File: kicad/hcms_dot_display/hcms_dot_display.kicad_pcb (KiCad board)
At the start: 2 copper layers, 35.5 x 19.8 mm, 35 parts, among them J1 Conn_01x13, J2 USB_C_Receptacle_USB2.0, J3 Conn_01x13, Q1 Q_PMOS_DSG, Q2 Q_PMOS_DSG, Q3 Q_PMOS_DSG, Q4 Q_PMOS_DSG, Q5 Q_PMOS_DSG, U1 ATtiny824-SSF, U2 FT231XS

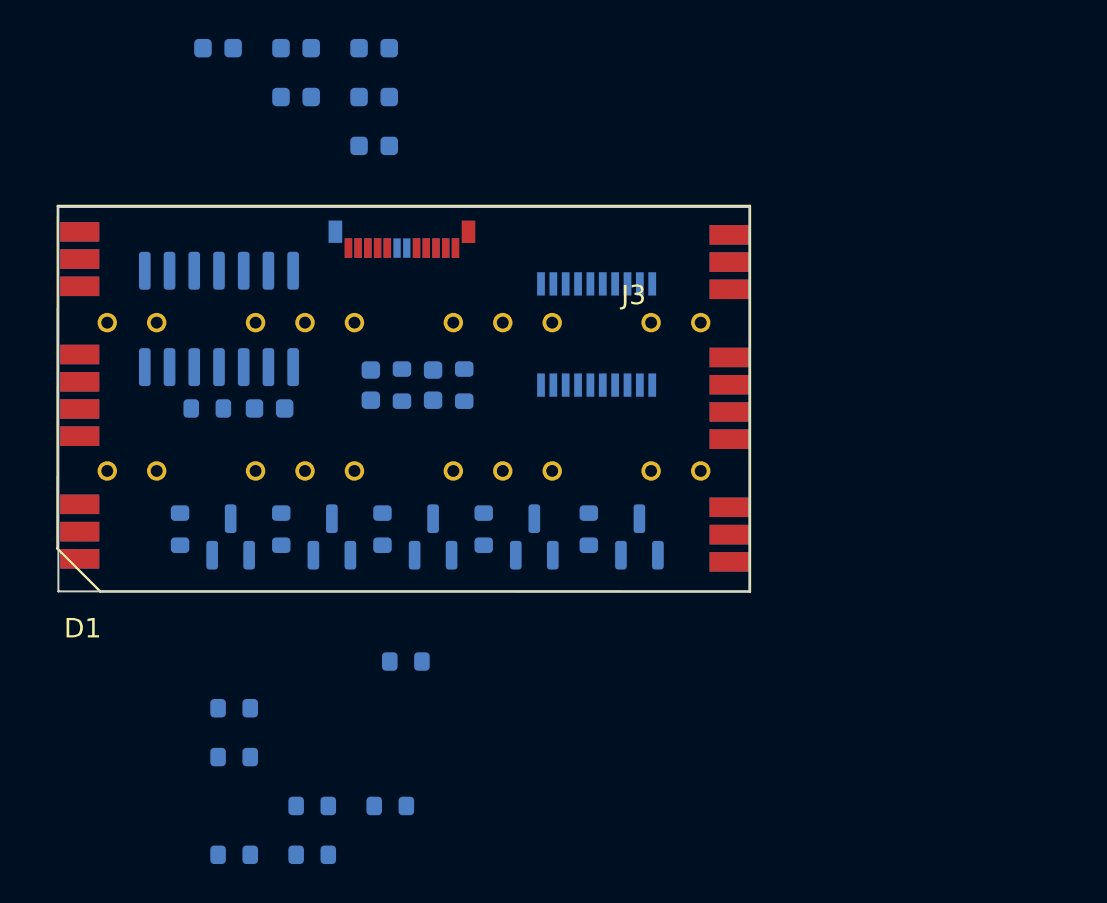
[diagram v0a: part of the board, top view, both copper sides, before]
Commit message: Added PNs for push button and pot with basic footprints, updated some resistor values
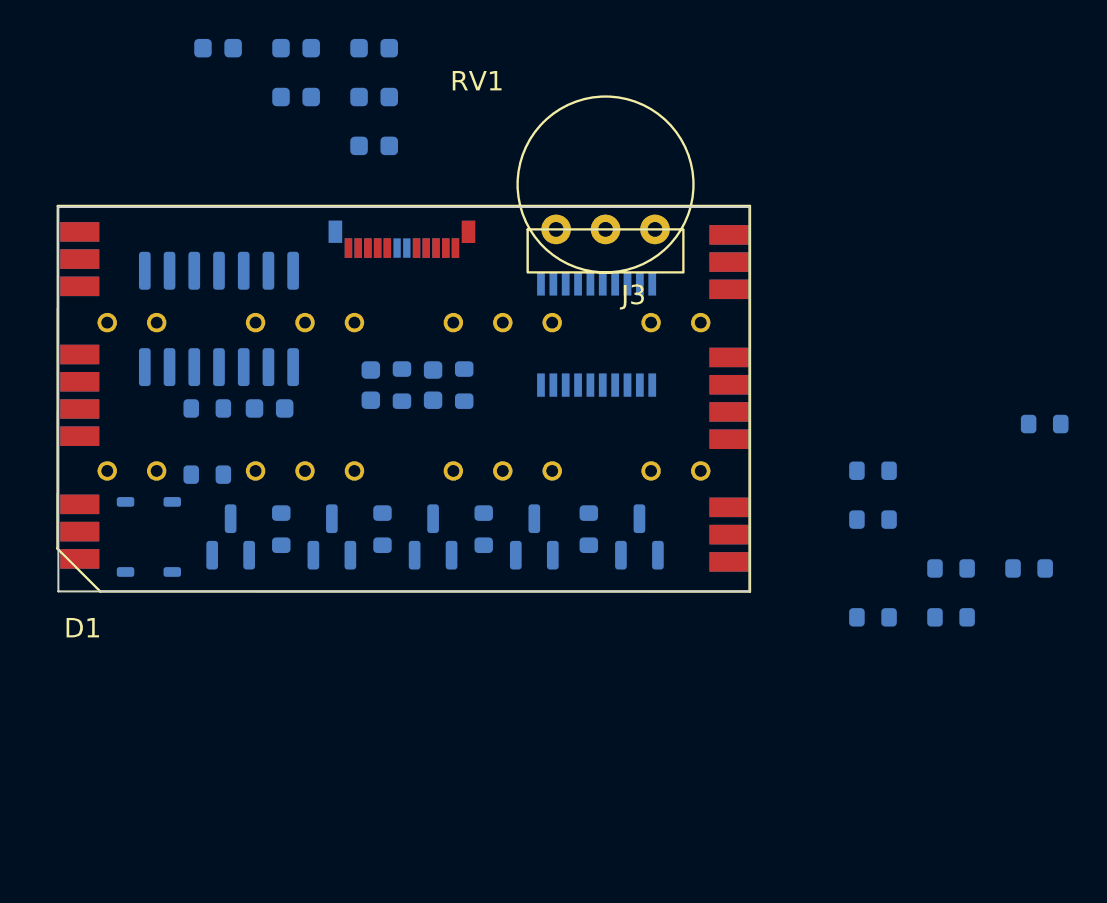
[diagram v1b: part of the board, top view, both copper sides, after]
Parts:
- added RV1: R_Potentiometer, hcms:3352T-1-503LF, F.Cu at (162.9, 97.4)
- added SW1: SW_Push, hcms:R-667845, B.Cu at (139.4, 113.2)
- R10, R11, R12, R13, R14: value R -> 200
- R3: value R -> 330
- moved R2 35.0 mm to (180.6, 114.8)
- moved R4 35.0 mm to (180.6, 117.3)
- moved R1 35.0 mm to (185.4, 107.4)
- moved R3 35.0 mm to (176.6, 112.3)
- moved R5 35.0 mm to (184.6, 114.8)
- moved R6 35.0 mm to (176.6, 117.3)
- moved R7 35.0 mm to (176.6, 109.8)
- moved R12 3.13 mm to (142.4, 110.0), turned to 180 degrees
- turned R13 to -90 degrees
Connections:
- J2 pad A4: +5V -> Net-(J2-PadA4)
- J2 pad A9: +5V -> Net-(J2-PadA4)
- J2 pad B4: +5V -> Net-(J2-PadA4)
- J2 pad B9: +5V -> Net-(J2-PadA4)
- R1 pad 1: Net-(D1-Pad26)_1 -> Net-(D1-Pad26)
- R2 pad 1: Net-(D1-Pad26)_1 -> Net-(D1-Pad26)
- R6 pad 1: Net-(D1-Pad26) -> Net-(D1-Pad26)_1
- R7 pad 1: Net-(D1-Pad26) -> Net-(D1-Pad26)_1

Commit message: layout
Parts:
- moved R5 46.7 mm to (142.8, 94.0)
- moved R1 46.4 mm to (139.0, 106.8)
- moved R3 42.4 mm to (138.4, 93.8)
- moved R2 42.1 mm to (139.0, 108.4)
- moved R4 41.6 mm to (146.2, 94.0)
- moved C7 25.0 mm to (157.8, 108.2)
- moved C9 20.4 mm to (154.6, 108.2)
- moved R7 15.7 mm to (161.0, 108.2)
- moved R6 15.4 mm to (164.2, 108.2)
- moved C6 13.3 mm to (158.6, 94.6)
- moved C8 11.9 mm to (162.6, 93.2)
- moved C1 9.73 mm to (140.0, 97.4)
- moved C2 9.05 mm to (143.0, 97.4)
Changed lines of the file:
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@@
   )
   (footprint "Capacitor_SMD:C_0603_1608Metric" (layer "B.Cu")
-    (at 142.951904 88.09 180)
+    (at 157.8 108.2 180)
     (descr "Capacitor SMD 0603 (1608 Metric), square (rectangular) end terminal, IPC_7351 nominal, (Body size source: IPC-SM-782 page 76, https://www.pcb-3d.com/wordpress/wp-content/uploads/ipc-sm-782a_amendment_1_and_2.pdf), generated with kicad-footprint-generator")
     (tags "capacitor")
@@
   )
   (footprint "Capacitor_SMD:C_0603_1608Metric" (layer "B.Cu")
-    (at 150.971904 88.09 180)
+    (at 154.6 108.2 180)
     (descr "Capacitor SMD 0603 (1608 Metric), square (rectangular) end terminal, IPC_7351 nominal, (Body size source: IPC-SM-782 page 76, https://www.pcb-3d.com/wordpress/wp-content/uploads/ipc-sm-782a_amendment_1_and_2.pdf), generated with kicad-footprint-generator")
     (tags "capacitor")
@@
   )
   (footprint "Resistor_SMD:R_0603_1608Metric" (layer "B.Cu")
-    (at 176.6 117.33 180)
+    (at 164.225 108.2 180)
     (descr "Resistor SMD 0603 (1608 Metric), square (rectangular) end terminal, IPC_7351 nominal, (Body size source: IPC-SM-782 page 72, https://www.pcb-3d.com/wordpress/wp-content/uploads/ipc-sm-782a_amendment_1_and_2.pdf), generated with kicad-footprint-generator")
     (tags "resistor")
@@
   )
   (footprint "Resistor_SMD:R_0603_1608Metric" (layer "B.Cu")
-    (at 176.6 112.31 180)
+    (at 138.4 93.8 180)
     (descr "Resistor SMD 0603 (1608 Metric), square (rectangular) end terminal, IPC_7351 nominal, (Body size source: IPC-SM-782 page 72, https://www.pcb-3d.com/wordpress/wp-content/uploads/ipc-sm-782a_amendment_1_and_2.pdf), generated with kicad-footprint-generator")
     (tags "resistor")
@@
   )
   (footprint "Capacitor_SMD:C_0603_1608Metric" (layer "B.Cu")
-    (at 146.961904 88.09 180)
+    (at 158.6 94.6 180)
     (descr "Capacitor SMD 0603 (1608 Metric), square (rectangular) end terminal, IPC_7351 nominal, (Body size source: IPC-SM-782 page 76, https://www.pcb-3d.com/wordpress/wp-content/uploads/ipc-sm-782a_amendment_1_and_2.pdf), generated with kicad-footprint-generator")
     (tags "capacitor")
@@
   )
   (footprint "Resistor_SMD:R_0603_1608Metric" (layer "B.Cu")
-    (at 180.61 117.33 180)
+    (at 146.2 94 180)
     (descr "Resistor SMD 0603 (1608 Metric), square (rectangular) end terminal, IPC_7351 nominal, (Body size source: IPC-SM-782 page 72, https://www.pcb-3d.com/wordpress/wp-content/uploads/ipc-sm-782a_amendment_1_and_2.pdf), generated with kicad-footprint-generator")
     (tags "resistor")
@@
   )
   (footprint "Capacitor_SMD:C_0603_1608Metric" (layer "B.Cu")
-    (at 150.971904 90.6 180)
+    (at 162.6 93.2 180)
     (descr "Capacitor SMD 0603 (1608 Metric), square (rectangular) end terminal, IPC_7351 nominal, (Body size source: IPC-SM-782 page 76, https://www.pcb-3d.com/wordpress/wp-content/uploads/ipc-sm-782a_amendment_1_and_2.pdf), generated with kicad-footprint-generator")
     (tags "capacitor")
@@
   )
   (footprint "Capacitor_SMD:C_0603_1608Metric" (layer "B.Cu")
-    (at 146.961904 90.6 180)
+    (at 140 97.4 180)
     (descr "Capacitor SMD 0603 (1608 Metric), square (rectangular) end terminal, IPC_7351 nominal, (Body size source: IPC-SM-782 page 76, https://www.pcb-3d.com/wordpress/wp-content/uploads/ipc-sm-782a_amendment_1_and_2.pdf), generated with kicad-footprint-generator")
     (tags "capacitor")
@@
   )
   (footprint "Resistor_SMD:R_0603_1608Metric" (layer "B.Cu")
-    (at 176.6 109.8 180)
+    (at 161 108.2 180)
     (descr "Resistor SMD 0603 (1608 Metric), square (rectangular) end terminal, IPC_7351 nominal, (Body size source: IPC-SM-782 page 72, https://www.pcb-3d.com/wordpress/wp-content/uploads/ipc-sm-782a_amendment_1_and_2.pdf), generated with kicad-footprint-generator")
     (tags "resistor")
@@
   )
   (footprint "Resistor_SMD:R_0603_1608Metric" (layer "B.Cu")
-    (at 180.61 114.82 180)
+    (at 139 108.4 180)
     (descr "Resistor SMD 0603 (1608 Metric), square (rectangular) end terminal, IPC_7351 nominal, (Body size source: IPC-SM-782 page 72, https://www.pcb-3d.com/wordpress/wp-content/uploads/ipc-sm-782a_amendment_1_and_2.pdf), generated with kicad-footprint-generator")
     (tags "resistor")
@@
   )
   (footprint "Capacitor_SMD:C_0603_1608Metric" (layer "B.Cu")
-    (at 150.971904 93.11 180)
+    (at 143 97.4 180)
     (descr "Capacitor SMD 0603 (1608 Metric), square (rectangular) end terminal, IPC_7351 nominal, (Body size source: IPC-SM-782 page 76, https://www.pcb-3d.com/wordpress/wp-content/uploads/ipc-sm-782a_amendment_1_and_2.pdf), generated with kicad-footprint-generator")
     (tags "capacitor")
@@
   )
   (footprint "Resistor_SMD:R_0603_1608Metric" (layer "B.Cu")
-    (at 184.62 114.82 180)
+    (at 142.8 94 180)
     (descr "Resistor SMD 0603 (1608 Metric), square (rectangular) end terminal, IPC_7351 nominal, (Body size source: IPC-SM-782 page 72, https://www.pcb-3d.com/wordpress/wp-content/uploads/ipc-sm-782a_amendment_1_and_2.pdf), generated with kicad-footprint-generator")
     (tags "resistor")
@@
   )
   (footprint "Resistor_SMD:R_0603_1608Metric" (layer "B.Cu")
-    (at 185.42 107.4 180)
-    (descr "Resistor SMD 0603 (1608 Metric), square (rectangular) end terminal, IPC_7351 nominal, (Body size source: IPC-SM-782 page 72, https://www.pcb-3d.com/wordpress/wp-content/uploads/ipc-sm-782a_amendment_1_and_2.pdf), generated with kicad-footprint-generator")
-    (tags "resistor")
+    (at 139 106.8 180)
+    (descr "Resistor SMD 0603 (1608 Metric), square (rectangular) end terminal, IPC_7351 nominal, (Body size source: IPC-SM-782 page 72, https://www.pcb-3d.com/wordpress/wp-content/uploads/ipc-sm-782a_amendment_1_and_2.pdf), generated with kicad-footprint-generator")
+    (tags "resistor")

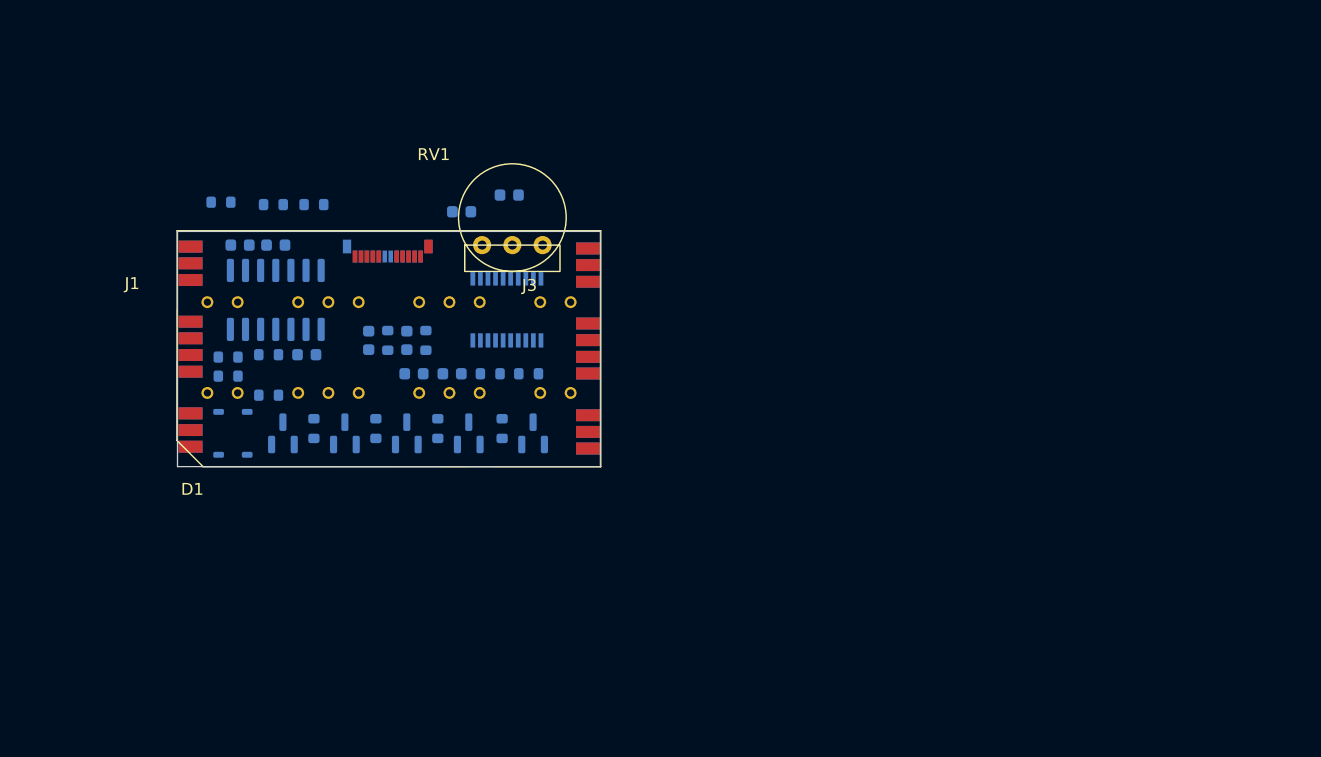
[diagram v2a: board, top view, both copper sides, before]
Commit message: Updated dot matrix footprint, experimented with stacked control board design
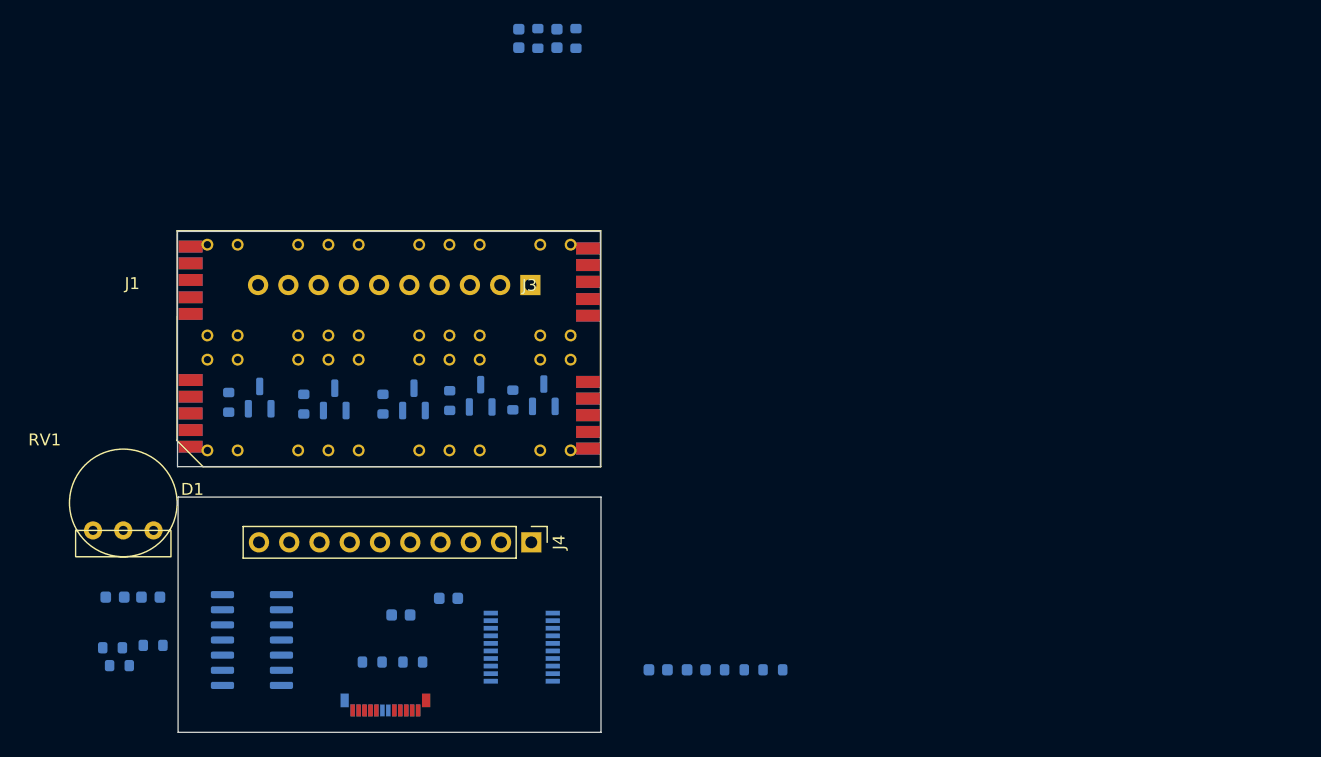
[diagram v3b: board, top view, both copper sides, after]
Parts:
- removed C3: 100nF, Capacitor_SMD:C_0603_1608Metric
- removed R3: 330, Resistor_SMD:R_0603_1608Metric
- removed SW1: SW_Push, hcms:R-667845
- added J4: Conn_01x13, Connector_PinHeader_2.54mm:PinHeader_1x10_P2.54mm_Vertical, F.Cu at (164.4, 122.3)
- added J5: Conn_01x13, Connector_PinHeader_2.54mm:PinHeader_1x10_P2.54mm_Vertical, B.Cu at (164.4, 100.8)
- R1, R6: value R -> 0
- R15: value R -> 1k
- R2, R7: value R -> DNP
- moved RV1 40.5 mm to (130.2, 121.3)
- moved R4 39.3 mm to (154.5, 132.4)
- moved R5 39.3 mm to (151.1, 132.4)
- moved J2 38.1 mm to (152.2, 136.5)
- moved C6 34.2 mm to (153.5, 128.4)
- moved C8 34.2 mm to (157.5, 127.0)
- moved C7 32.2 mm to (178.3, 133.1)
- moved C9 32.2 mm to (175.1, 133.1)
- moved R6 32.2 mm to (184.7, 133.1)
- moved R7 32.2 mm to (181.5, 133.1)
- moved C1 31.4 mm to (129.5, 127.0)
- moved C2 31.4 mm to (132.5, 127.0)
- moved U1 28.6 mm to (141.0, 130.6), turned to 0 degrees
- moved U2 28.4 mm to (163.7, 131.2), turned to 180 degrees
- moved C4 28.3 mm to (166.6, 80.0)
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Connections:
- R1 pad 1: Net-(D1-Pad26) -> Net-(D1-Pad26A)
- R2 pad 1: Net-(D1-Pad26) -> Net-(D1-Pad26A)
- R6 pad 1: Net-(D1-Pad26)_1 -> Net-(R6-Pad1)
- R7 pad 1: Net-(D1-Pad26)_1 -> Net-(R6-Pad1)
- U1 pad 10: /UPDI -> /MCU_COL_3
- U1 pad 11: /MCU_COL_1 -> /MCU_COL_2
- U1 pad 12: /MCU_COL_2 -> /MCU_COL_1
- U1 pad 13: /MCU_COL_3 -> /UPDI
- U1 pad 2: /MCU_COL_4 -> /MCU_DATA
- U1 pad 3: /MCU_COL_5 -> unconnected-(U1-Pad3)
- U1 pad 4: /POT -> /nBLNK
- U1 pad 5: /CLK -> unconnected-(U1-Pad5)
- U1 pad 6: /nBLNK -> /POT
- U1 pad 7: unconnected-(U1-Pad7) -> /CLK
- U1 pad 8: unconnected-(U1-Pad8) -> /MCU_COL_5
- U1 pad 9: /MCU_DATA -> /MCU_COL_4
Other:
- board size 35.5 x 19.8 mm -> 35.6 x 42.1 mm

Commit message: Cleaned up layout strat
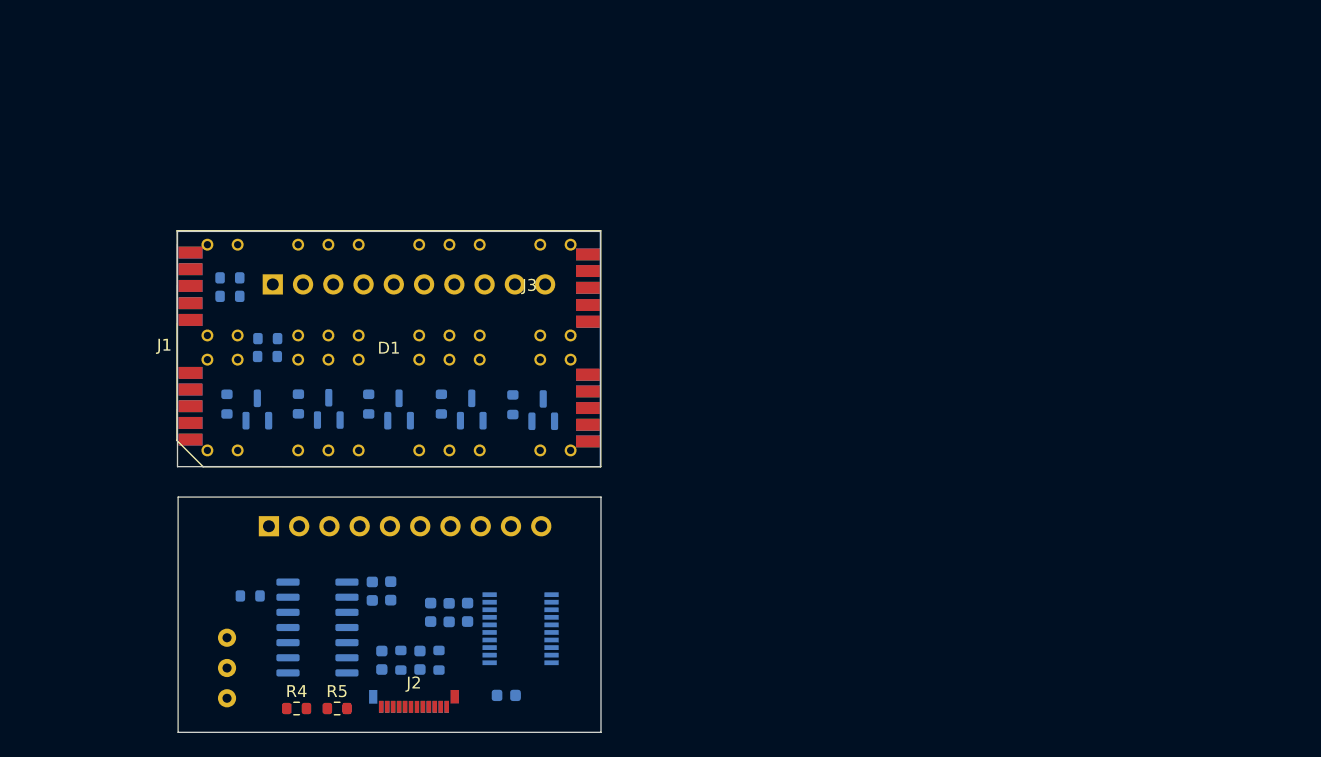
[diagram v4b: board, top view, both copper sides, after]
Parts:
- J2, R4, R5: moved to F.Cu
- J4: value Conn_01x13 -> Conn_01x10_Female; moved to B.Cu
- J5: value Conn_01x13 -> Conn_01x10_Male
- RV1: moved to B.Cu
- moved R6 55.3 mm to (139.2, 101.7)
- moved R7 53.6 mm to (139.2, 100.2)
- moved C4 53.5 mm to (155.1, 132.2)
- moved C5 53.5 mm to (151.9, 132.2)
- moved R8 53.5 mm to (156.7, 132.2)
- moved R9 53.5 mm to (153.5, 132.2)
- moved J4 30.7 mm to (142.8, 100.7)
- moved J5 29.9 mm to (142.4, 121.0), turned to -90 degrees
- moved R1 29.0 mm to (142.3, 105.2)
- moved R2 28.8 mm to (142.3, 106.8)
- moved C1 21.6 mm to (151.1, 126.5), turned to -90 degrees
- moved C7 21.3 mm to (157.6, 128.2), turned to 90 degrees
- moved C2 20.2 mm to (152.7, 126.4), turned to -90 degrees
- moved C9 16.7 mm to (159.1, 128.2), turned to 90 degrees
- moved RV1 14.5 mm to (138.9, 132.9), turned to -90 degrees
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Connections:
- J4 pad 1: unconnected-(J4-Pad1) -> /nBLNK
- J4 pad 10: unconnected-(J4-Pad10) -> GND
- J4 pad 2: unconnected-(J4-Pad2) -> /MCU_DATA
- J4 pad 3: unconnected-(J4-Pad3) -> /CLK
- J4 pad 4: unconnected-(J4-Pad4) -> /MCU_COL_5
- J4 pad 5: unconnected-(J4-Pad5) -> /MCU_COL_4
- J4 pad 6: unconnected-(J4-Pad6) -> /MCU_COL_3
- J4 pad 7: unconnected-(J4-Pad7) -> /MCU_COL_2
- J4 pad 8: unconnected-(J4-Pad8) -> /MCU_COL_1
- J4 pad 9: unconnected-(J4-Pad9) -> +5V
- J5 pad 1: unconnected-(J5-Pad1) -> /nBLNK
- J5 pad 10: unconnected-(J5-Pad10) -> GND
- J5 pad 2: unconnected-(J5-Pad2) -> /MCU_DATA
- J5 pad 3: unconnected-(J5-Pad3) -> /CLK
- J5 pad 4: unconnected-(J5-Pad4) -> /MCU_COL_5
- J5 pad 5: unconnected-(J5-Pad5) -> /MCU_COL_4
- J5 pad 6: unconnected-(J5-Pad6) -> /MCU_COL_3
- J5 pad 7: unconnected-(J5-Pad7) -> /MCU_COL_2
- J5 pad 8: unconnected-(J5-Pad8) -> /MCU_COL_1
- J5 pad 9: unconnected-(J5-Pad9) -> +5V
